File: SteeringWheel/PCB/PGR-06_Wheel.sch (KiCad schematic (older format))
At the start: 37 parts

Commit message: New Steering wheel scheme
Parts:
- removed 1k, 1k? (x23): 1k, symbol Device:R_Small
- removed C?: 1uF, symbol Device:C_Small
- removed D? (x2): LED_BGCR, symbol Device:LED_BGCR
- removed JP?: Jumper_NO_Small, symbol Device:Jumper_NO_Small
- removed R?: R_Small, symbol Device:R_Small
- removed R?: 120 Ohm, symbol Device:R_Small
- removed ScreenChg_RotarySwitch: SW_Rotary6, symbol Switch:SW_Rotary6
- removed TCS_RotarySwitch, Uni_RotarySwitch: SW_Rotary10, symbol Switch:SW_Rotary10
- removed U?: STM32F105RBTx, Package_QFP:LQFP-64_10x10mm_P0.5mm, symbol MCU_ST_STM32F1:STM32F105RBTx
- removed U?: MCP2551-I-SN, Package_SO:SOIC-8_3.9x4.9mm_P1.27mm, symbol Interface_CAN_LIN:MCP2551-I-SN
- added C1, C?: C_Small, symbol Device:C_Small
- added CLCH_Button1, DRS_Button1, UNI1_Button1, UNI2_Button1: SW_Push, symbol Switch:SW_Push
- added Clutch, J?: Conn_01x06_Male, symbol Connector:Conn_01x06_Male
- added D? (x2): WS2812B, LED_SMD:LED_WS2812B_PLCC4_5.0x5.0mm_P3.2mm, symbol LED:WS2812B
- added DebugConn: Conn_01x05_Male, symbol Connector:Conn_01x05_Male
- added U1, U?: MCP2561-E-SN, Package_SO:SOIC-8_3.9x4.9mm_P1.27mm, symbol Interface_CAN_LIN:MCP2561-E-SN
- renumbered PTT_Button to PTT_Button1, ScreenChg_Button to SCR_CHG_Button1
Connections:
- net labels added: +12V, CAN1_RX, CAN1_TX, CAN2_RX, CAN2_TX, CLK, CS_P6, DO_P4
- net labels removed: +3.3VA, BOOT0, NRST
- wire segments 135 -> 27
- no-connect marks 0 -> 2
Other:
- moved on the sheet: PTT_Button1, SCR_CHG_Button1

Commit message: Steering Wheel Update
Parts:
- removed Clutch, J?: Conn_01x06_Male, symbol Connector:Conn_01x06_Male
- added 100uF1, 100uF2, 1uF1, 1uF2: C_Small, Capacitor_SMD:C_0603_1608Metric, symbol Device:C_Small
- added 10k1, 10k2: R_Small, Resistor_SMD:R_0805_2012Metric, symbol Device:R_Small
- added 330uH1, 330uH2: L_Small, PGR-06_Additional:7447707331, symbol Device:L_Small
- added C3, C5: 16SVPG330MX, 16SVPG330MX:CAP_16SVPG330MX, symbol 16SVPG330MX:16SVPG330MX
- added Clutch1, MAIN1: 22-05-7065, 22-05-7065:22057065, symbol 22-05-7065:22-05-7065
- added D1, D4: 1N5819, Diode_THT:D_DO-41_SOD81_P10.16mm_Horizontal, symbol Diode:1N5819
- added IC1: LM2575HVS-5.0_NOPB, LM2575HVS-5.0_NOPB:TO170P1435X465-6N, symbol LM2575HVS-5.0_NOPB:LM2575HVS-5.0_NOPB
- added NHD-C0220BiZ1: NHD-C0220BiZ-FS(RGB)-FBW-3VM, PGR-06_Additional:NHD-C0220BiZ-FS(RGB)-FBW-3VM, symbol PGR-06_Wheel_Additional:NHD-C0220BiZ-FS(RGB)-FBW-3VM
- added U3: LM2575HVS-3.3_NOPB, LM2575HVS-3.3_NOPB:VREG_TPS79625KTTR, symbol LM2575HVS-3.3_NOPB:LM2575HVS-3.3_NOPB
- C1: footprint (none) -> Capacitor_SMD:C_0603_1608Metric
- C2: renamed from C?; footprint (none) -> Capacitor_SMD:C_0603_1608Metric
- CLCH_Button1, DRS_Button1, PTT_Button1, SCR_CHG_Button1, UNI1_Button1, UNI2_Button1: footprint (none) -> Connector_Wire:SolderWire-2sqmm_1x02_P7.8mm_D2mm_OD3.9mm
- DebugConn1: renamed from DebugConn; footprint (none) -> Connector_PinHeader_2.54mm:PinHeader_1x05_P2.54mm_Vertical
- gave numbers to parts that had none: 3
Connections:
- net labels added: CAN1_H, CAN1_L, CAN2_H, CAN2_L
- net labels removed: CANH, CANL
- wire segments 27 -> 66

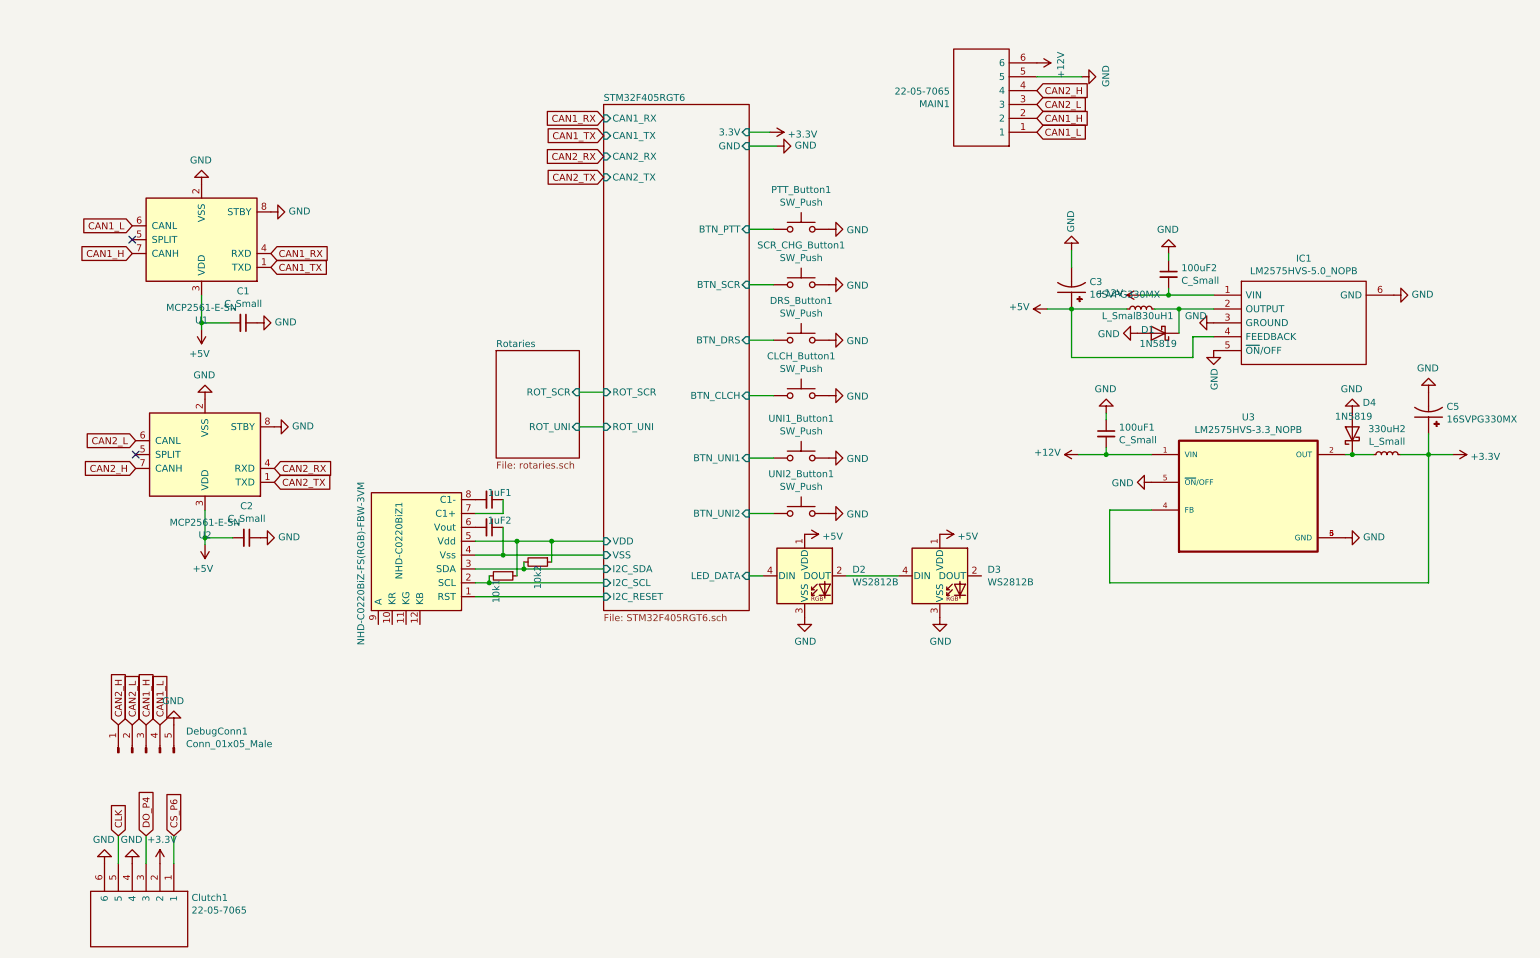
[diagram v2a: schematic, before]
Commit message: New brd for steering wheel
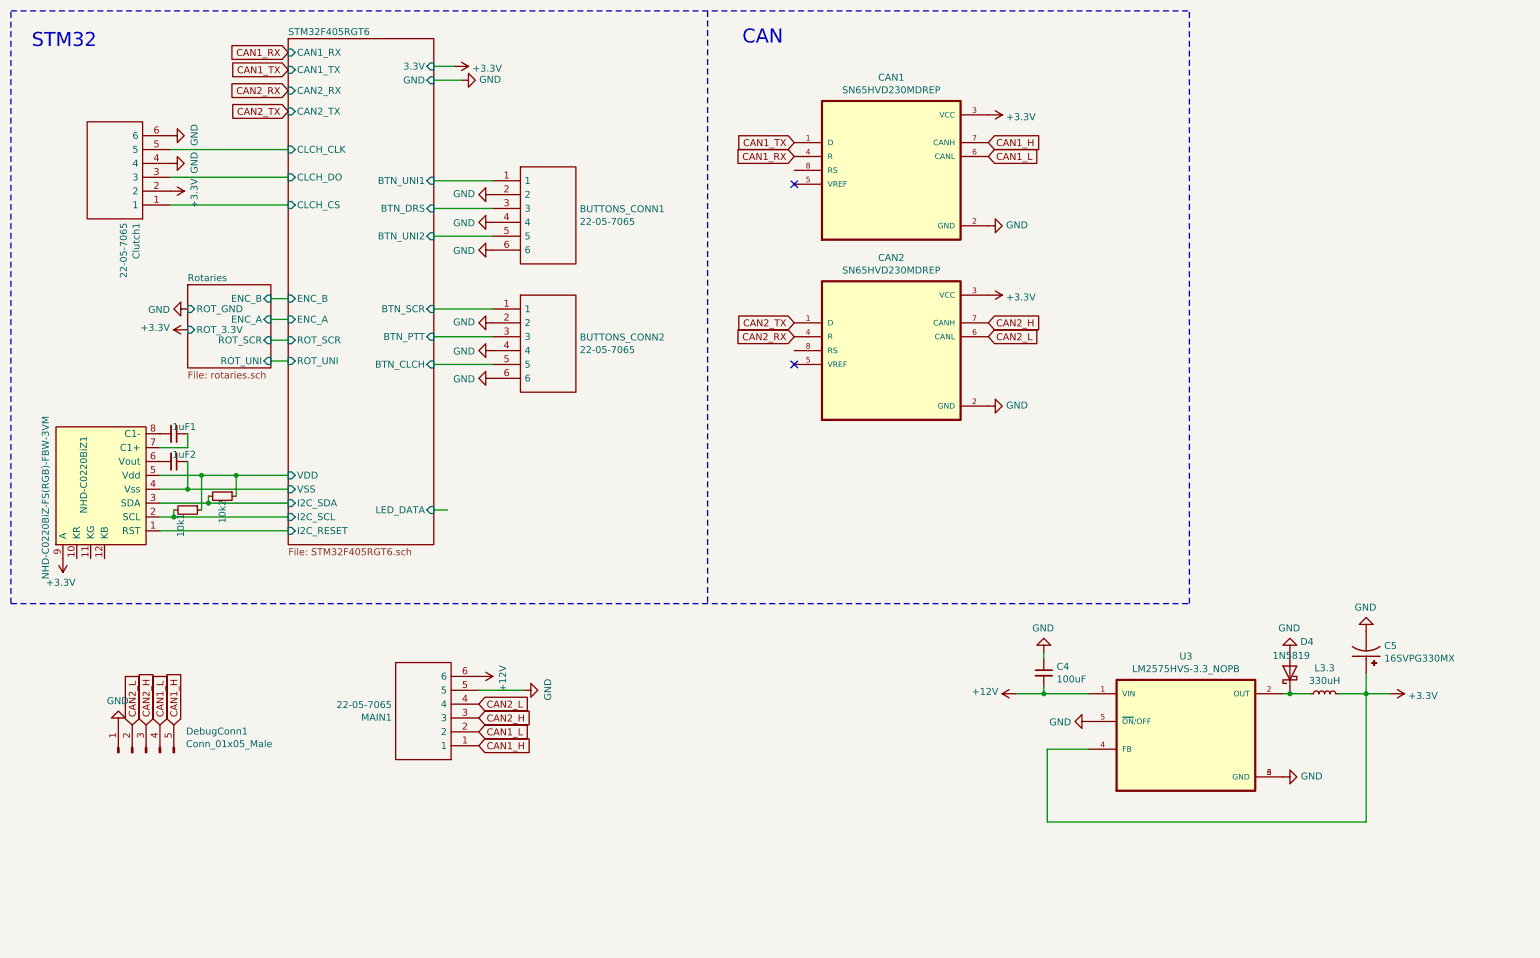
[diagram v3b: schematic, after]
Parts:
- removed 100uF2, C1, C2: C_Small, Capacitor_SMD:C_0603_1608Metric, symbol Device:C_Small
- removed 330uH1: L_Small, PGR-06_Additional:7447707331, symbol Device:L_Small
- removed C3: 16SVPG330MX, 16SVPG330MX:CAP_16SVPG330MX, symbol 16SVPG330MX:16SVPG330MX
- removed CLCH_Button1, DRS_Button1, PTT_Button1, SCR_CHG_Button1, UNI1_Button1, UNI2_Button1: SW_Push, Connector_Wire:SolderWire-2sqmm_1x02_P7.8mm_D2mm_OD3.9mm, symbol Switch:SW_Push
- removed D1: 1N5819, Diode_THT:D_DO-41_SOD81_P10.16mm_Horizontal, symbol Diode:1N5819
- removed D2, D3: WS2812B, LED_SMD:LED_WS2812B_PLCC4_5.0x5.0mm_P3.2mm, symbol LED:WS2812B
- removed IC1: LM2575HVS-5.0_NOPB, LM2575HVS-5.0_NOPB:TO170P1435X465-6N, symbol LM2575HVS-5.0_NOPB:LM2575HVS-5.0_NOPB
- removed U1, U2: MCP2561-E-SN, Package_SO:SOIC-8_3.9x4.9mm_P1.27mm, symbol Interface_CAN_LIN:MCP2561-E-SN
- added BUTTONS_CONN1, BUTTONS_CONN2: 22-05-7065, 22-05-7065:22057065, symbol 22-05-7065:22-05-7065
- added CAN1, CAN2: SN65HVD230MDREP, PGR-06_Additional:SOIC127P599X175-8N, symbol PGR-06_Wheel_Additional:SN65HVD230MDREP
- C4: renamed from 100uF1; value C_Small -> 100uF
- D4: footprint Diode_THT:D_DO-41_SOD81_P10.16mm_Horizontal -> Diode_SMD:D_SMC
- L3.3: renamed from 330uH2; value L_Small -> 330uH
- NHD-C0220BiZ1: footprint PGR-06_Additional:NHD-C0220BiZ-FS(RGB)-FBW-3VM -> PGR-06_Additional:NHD-C0220BiZ-FS(RGB)-FBW-3VM-NEW
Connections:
- net +3V3: now also NHD-C0220BiZ1.9 (A), CAN1.3 (VCC), CAN2.3 (VCC)
- net CAN1_H: now also DebugConn1.5 (Pin_5), MAIN1.1, CAN1.7 (CANH); no longer DebugConn1.3 (Pin_3), MAIN1.2
- net CAN1_L: now also MAIN1.2, CAN1.6 (CANL); no longer MAIN1.1
- net CAN1_RX: now also CAN1.4 (R)
- net CAN1_TX: now also CAN1.1 (D)
- net CAN2_H: now also DebugConn1.3 (Pin_3), MAIN1.3, CAN2.7 (CANH); no longer DebugConn1.1 (Pin_1), MAIN1.4
- net CAN2_L: now also MAIN1.4, CAN2.6 (CANL); no longer MAIN1.3
- net CAN2_RX: now also CAN2.4 (R)
- net CAN2_TX: now also CAN2.1 (D)
- net GND: now also DebugConn1.1 (Pin_1), BUTTONS_CONN1.2, BUTTONS_CONN1.4, BUTTONS_CONN1.6, BUTTONS_CONN2.2, BUTTONS_CONN2.4, BUTTONS_CONN2.6, CAN1.2 (GND), CAN2.2 (GND); no longer DebugConn1.5 (Pin_5)
- net STM32F405RGT6/BTN_CLCH: now also BUTTONS_CONN2.5
- net STM32F405RGT6/BTN_DRS: now also BUTTONS_CONN1.3
- net STM32F405RGT6/BTN_PTT: now also BUTTONS_CONN2.3
- net STM32F405RGT6/BTN_SCR: now also BUTTONS_CONN2.1
- net STM32F405RGT6/BTN_UNI1: now also BUTTONS_CONN1.1
- net STM32F405RGT6/BTN_UNI2: now also BUTTONS_CONN1.5
- net CLK renamed STM32F405RGT6/CLCH_CLK
- net CS_P6 renamed STM32F405RGT6/CLCH_CS
- net DO_P4 renamed STM32F405RGT6/CLCH_DO
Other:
- note added: "CAN"
- note added: "STM32\n"
- moved on the sheet: 10k1, 10k2, 1uF1, 1uF2, C4, C5, Clutch1, D4, L3.3, MAIN1, NHD-C0220BiZ1, U3

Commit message: Steering Wheel Update
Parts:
- removed C4: 100uF, Capacitor_SMD:C_0603_1608Metric, symbol Device:C_Small
- removed C5: 16SVPG330MX, 16SVPG330MX:CAP_16SVPG330MX, symbol 16SVPG330MX:16SVPG330MX
- removed CAN1, CAN2: SN65HVD230MDREP, PGR-06_Additional:SOIC127P599X175-8N, symbol PGR-06_Wheel_Additional:SN65HVD230MDREP
- removed D4: 1N5819, Diode_SMD:D_SMC, symbol Diode:1N5819
- removed L3.3: 330uH, PGR-06_Additional:7447707331, symbol Device:L_Small
- removed U3: LM2575HVS-3.3_NOPB, LM2575HVS-3.3_NOPB:VREG_TPS79625KTTR, symbol LM2575HVS-3.3_NOPB:LM2575HVS-3.3_NOPB
- added C1: BD_CAP2, Capacitor_SMD:C_0805_2012Metric, symbol Device:C_Small
- added C2: BD_CAP1, Capacitor_SMD:C_0805_2012Metric, symbol Device:C_Small
- added CAN1, CAN2: MCP2561-E-P, Package_DIP:DIP-8_W7.62mm, symbol Interface_CAN_LIN:MCP2561-E-P
- added DI1: 0Ohm, Resistor_SMD:R_0805_2012Metric, symbol Device:R_Small
- added H1, H2, H3: MountingHole, MountingHole:MountingHole_3.2mm_M3, symbol Mechanical:MountingHole
- added H4: MountingHole_Pad, MountingHole:MountingHole_3.2mm_M3_Pad_TopBottom, symbol Mechanical:MountingHole_Pad
- added IC_33v1: BD733L5FP-CE2, PGR-06_Additional:BD750L5FPCE2, symbol PGR-06_Wheel_Additional:BD733L5FP-CE2
- added LED_B1, LED_G1, LED_R1: R_Small, Resistor_SMD:R_0805_2012Metric, symbol Device:R_Small
- added R_Terminator_1, R_Terminator_2: 120Ohm, Resistor_SMD:R_0805_2012Metric, symbol Device:R_Small
- added U1: LM1117-5.0, Package_TO_SOT_SMD:TO-252-2, symbol Regulator_Linear:LM1117-5.0
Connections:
- net +3V3: now also C2.1, IC_33v1.3 (VOUT)
- net CAN1_H: now also MAIN1.4, CAN1.7 (CANH), R_Terminator_1.1; no longer MAIN1.1
- net CAN1_L: now also MAIN1.3, CAN1.6 (CANL), R_Terminator_1.2; no longer MAIN1.2
- net CAN1_RX: now also CAN1.4 (RXD)
- net CAN1_TX: now also CAN1.1 (TXD)
- net CAN2_H: now also MAIN1.2, CAN2.7 (CANH), R_Terminator_2.1; no longer MAIN1.3
- net CAN2_L: now also MAIN1.1, CAN2.6 (CANL), R_Terminator_2.2; no longer MAIN1.4
- net CAN2_RX: now also CAN2.4 (RXD)
- net CAN2_TX: now also CAN2.1 (TXD)
- net GND: now also C1.1, C2.2, CAN1.2 (VSS), CAN1.8 (STBY), CAN2.2 (VSS), CAN2.8 (STBY), H4.1, IC_33v1.4 (GND), U1.1 (GND)
- net at NHD-C0220BiZ1.10 (KR): now also LED_R1.2
- net at NHD-C0220BiZ1.11 (KG): now also LED_G1.2
- net at NHD-C0220BiZ1.12 (KB): now also LED_B1.2
- net +12V renamed VDD
- net VDD: now also C1.2, DI1.1, IC_33v1.1 (VCC), U1.3 (VI)
- new net +5V: CAN1.3 (VDD), CAN2.3 (VDD), DI1.2, U1.2 (VO)
- new net STM32F405RGT6/LED_B: LED_B1.1
- new net STM32F405RGT6/LED_G: LED_G1.1
- new net STM32F405RGT6/LED_R: LED_R1.1
